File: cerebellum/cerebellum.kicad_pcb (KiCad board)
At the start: 2 copper layers, 91.5 x 52 mm, 82 parts, among them J1 PowerIn, J2 UART, J3 SWD_DBG, J4 SWD_DBG_PIN, J5 CAN FD, J6 CAN, Q1 AP2300, U1 OK1061-S, U2 TPS5430DDA, U3 BMI088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

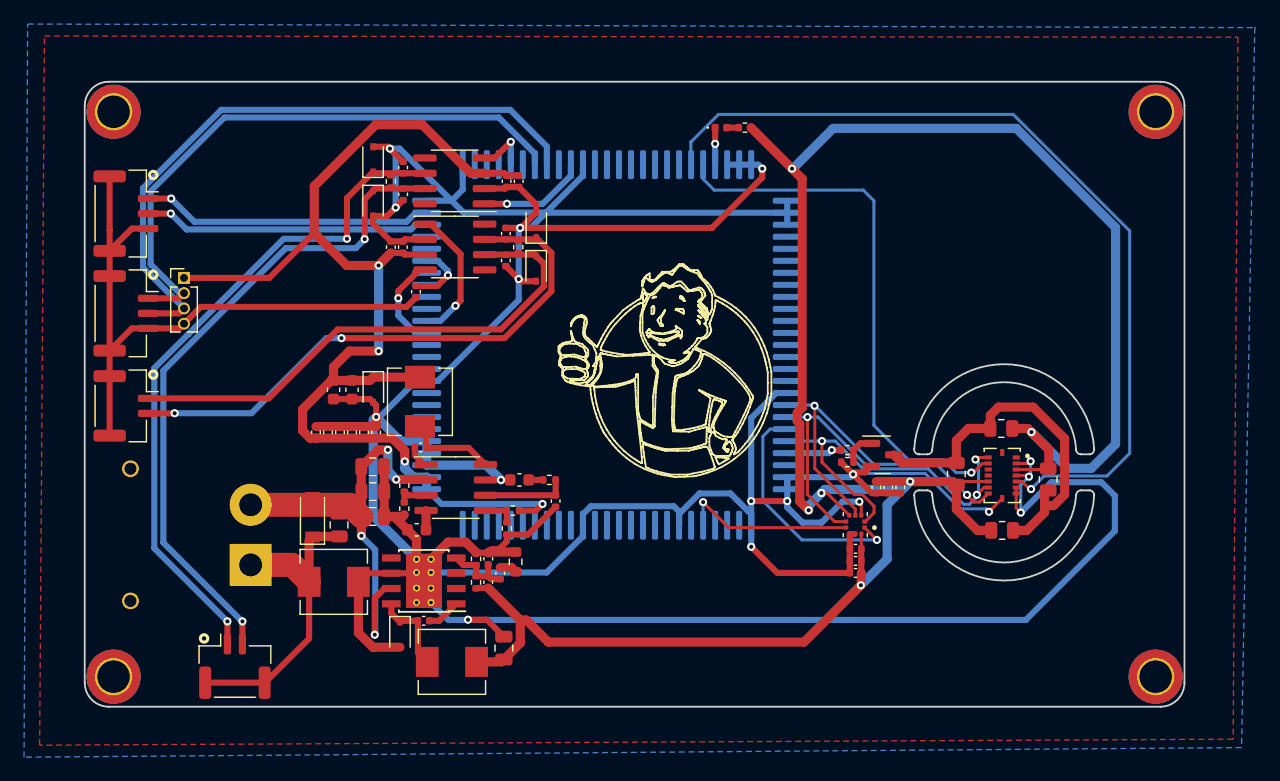
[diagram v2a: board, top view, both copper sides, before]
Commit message: [Modify] Replace DCDC(24to3V3) to LDO(5to3V3)
Signed-off-by: Homalozoa <nx.tardis@gmail.com>
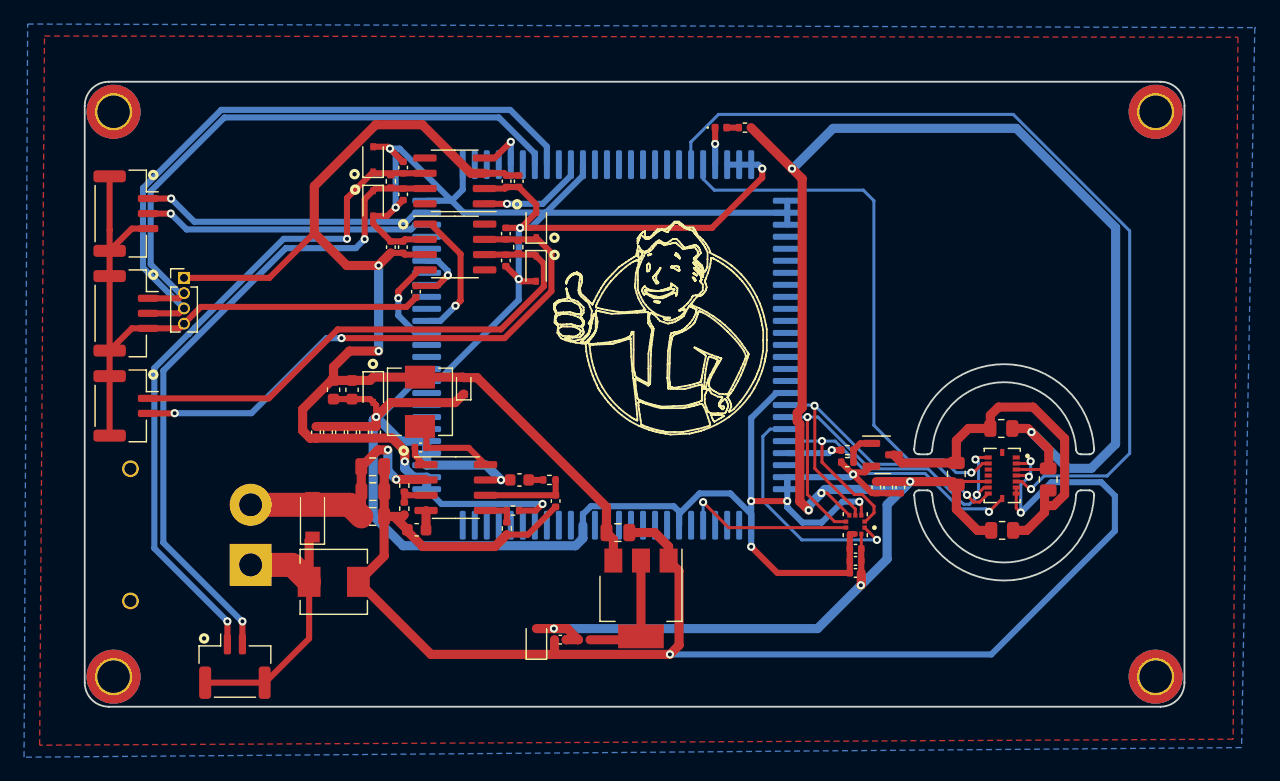
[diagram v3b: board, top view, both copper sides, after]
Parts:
- removed C19: 100uf/6.3V/0805, Capacitor_SMD:C_0805_2012Metric
- removed C21: 1.5nf/50V/0402, Capacitor_SMD:C_0402_1005Metric
- removed C24: 100nf/50V/0402, Capacitor_SMD:C_0402_1005Metric
- removed C28: 150pf/50V/0402, Capacitor_SMD:C_0402_1005Metric
- removed R11: 549R/0603, Resistor_SMD:R_0603_1608Metric
- removed R6: 10k/0402, Resistor_SMD:R_0402_1005Metric
- removed R7: 5.9k/0402, Resistor_SMD:R_0402_1005Metric
- added D9: PTVSLC3D3V3B, Diode_SMD:D_SOD-323, F.Cu at (141.8, 120.5)
- C13: value 4.7uF/50V/0805 -> 10uf/50V/0805
- C17: value 10nf/50V/0402 -> 22uf/6.3V/0402
- D2: value BZT52C3V3S -> TVSS5VCES-02GP; footprint Diode_SMD:D_SOD-323 -> Diode_SMD:D_SOD-523
- L2: value 15uh/SLO0530H150MTT -> MLG1005S1N3BT000; footprint Inductor_SMD:L_Sunlord_MWSA0518_5.4x5.2mm -> Inductor_SMD:L_0402_1005Metric
- U2: value TPS5430DDA -> AMS1117-3.3; footprint Package_SO:TI_SO-PowerPAD-8_ThermalVias -> Package_TO_SOT_SMD:SOT-223-3_TabPin2
- moved C13 23.2 mm to (148.6, 111.5), turned to 0 degrees
- moved D2 21.3 mm to (135.8, 99.3), turned to 90 degrees
- moved U2 18.1 mm to (150.5, 117.0), turned to -90 degrees
- moved C17 11.5 mm to (143.8, 120.4)
- moved L2 11.2 mm to (145.8, 120.4)
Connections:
- C13 pad 1: +24V -> +5V
- C13 pad 2: GNDA -> GND
- C17 pad 1: Net-(C17-Pad1) -> +3V3
- C17 pad 2: Net-(C17-Pad2) -> GND
- D2 pad 1: Net-(C17-Pad2) -> GND
- D2 pad 2: GND -> +5V
- L2 pad 1: +3V3 -> Net-(L2-Pad1)
- L2 pad 2: Net-(C17-Pad2) -> +3V3
- U2 pad 1: Net-(C17-Pad1) -> GND
- U2 pad 2: unconnected-(U2-Pad2) -> Net-(L2-Pad1)
- U2 pad 3: unconnected-(U2-Pad3) -> +5V
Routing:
- net +5V: track 99.2 -> 123.9 mm
- net GND: track 435.0 -> 453.1 mm
- net +24V: track 37.6 -> 22.6 mm, vias 4 -> 2
- net Net-(L2-Pad1): track 0.00 -> 10.7 mm
- net +3V3: track 185.6 -> 175.5 mm, vias 6 -> 7
- net Net-(C17-Pad2): track 6.95 -> 0.00 mm
- net TPS_VSEN: track 5.92 -> 0.00 mm
- net Net-(C17-Pad1): track 2.82 -> 0.00 mm
- net GNDA: track 26.4 -> 24.2 mm
- net Net-(C24-Pad2): track 1.43 -> 0.00 mm
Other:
- board text added: "Rev.v2"

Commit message: [Modify] Change pressure sensor to MPL3115A2R1
Signed-off-by: Homalozoa <nx.tardis@gmail.com>
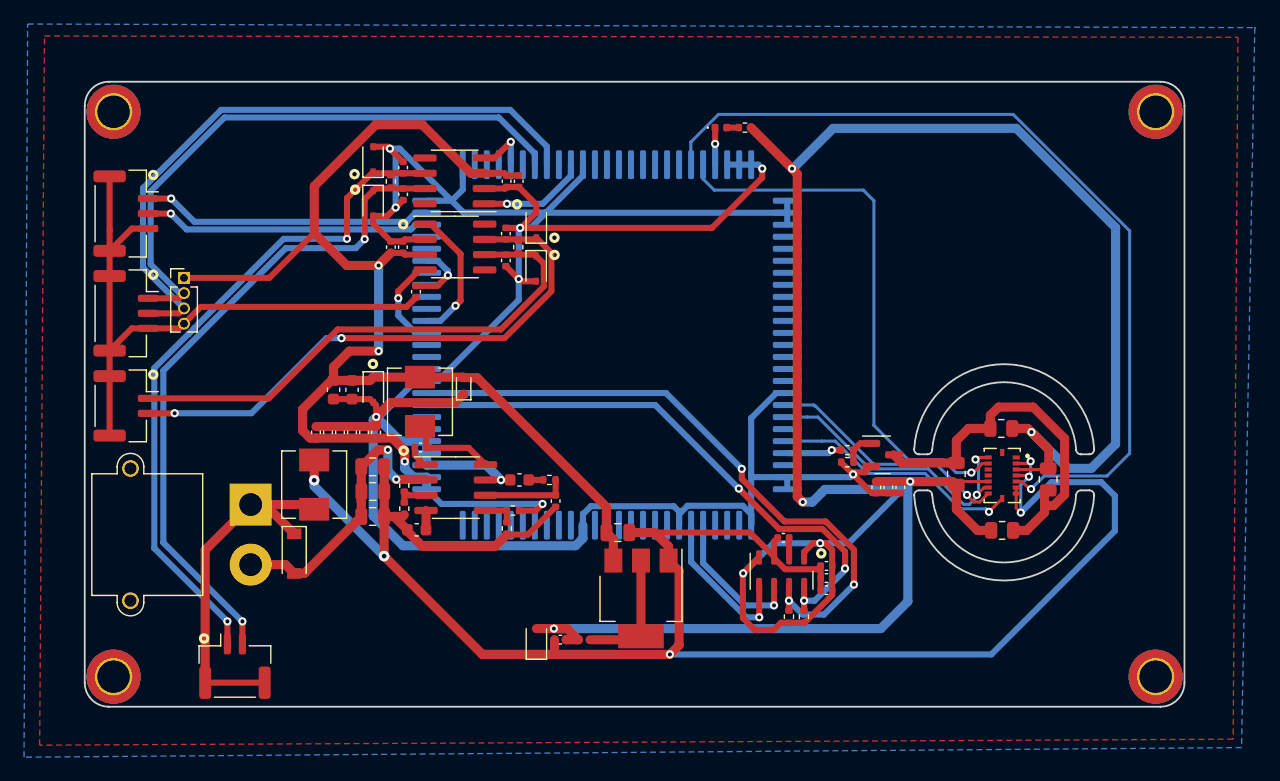
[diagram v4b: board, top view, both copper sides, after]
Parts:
- added C19: 100nF/10V/0402, Capacitor_SMD:C_0402_1005Metric, F.Cu at (162.4, 112.0)
- added R6: 1k/0402, Resistor_SMD:R_0402_1005Metric, F.Cu at (162.8, 118.5)
- added R7: 1k/0402, Resistor_SMD:R_0402_1005Metric, F.Cu at (164.1, 118.5)
- C31: value 4.7uF/10V/0402 -> 100nF/10V/0402
- C32: value 100nF/10V/0402 -> 1uF/10V/0402
- C51: value 100nF/10V/0402 -> 10uF/10V/0402
- J1: moved to F.Cu
- J2: value UART -> GH1.25-3PLTPZ
- J4: value SWD_DBG_PIN -> GH1.25-3PLTPZ
- J5: value CAN FD -> GH1.25-2PWBPZ
- J6: value CAN -> GH1.25-2PWBPZ
- U5: value ICP-20100 -> MPL3115A2; footprint Rolling_Custom:PQFN50P200X200X85-10N -> Package_LGA:NXP_LGA-8_3x5mm_P1.25mm_H1.1mm
- moved L3 8.25 mm to (123.3, 107.5), turned to -90 degrees
- moved U5 7.25 mm to (162.2, 114.7), turned to -90 degrees
- moved J1 5.02 mm to (118.1, 109.2), turned to 90 degrees
- moved D1 3.39 mm to (121.7, 113.3), turned to -90 degrees
- moved C31 2.81 mm to (166.0, 114.3)
- moved C32 2.81 mm to (166.0, 115.3)
- moved C51 2.81 mm to (166.0, 116.3)
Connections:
- U1 pad 70: ICP_SCS -> unconnected-(U1-Pad70)
- U1 pad 8: unconnected-(U1-Pad8) -> PRE_SDA
- U1 pad 80: ICP_INT -> PRE_INT1
- U1 pad 81: unconnected-(U1-Pad81) -> PRE_INT2
- U1 pad 9: unconnected-(U1-Pad9) -> PRE_SCL
- U5 pad 1: ICP_SCS -> +3V3
- U5 pad 2: SENSOR_SCK -> Net-(C19-Pad2)
- U5 pad 4: SENSOR_SDI -> +3V3
- U5 pad 5: +3V3 -> PRE_INT2
- U5 pad 6: SENSOR_SDO -> PRE_INT1
- U5 pad 7: ICP_INT -> PRE_SCL
- U5 pad 8: GND -> PRE_SDA
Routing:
- net PRE_SCL: track 0.00 -> 53.4 mm, vias 0 -> 3
- net PRE_SDA: track 0.00 -> 48.0 mm, vias 0 -> 3
- net +3V3: track 175.5 -> 208.8 mm
- net ICP_SCS: track 19.9 -> 0.00 mm, vias 1 -> 0
- net ICP_INT: track 14.7 -> 0.00 mm, vias 1 -> 0
- net PRE_INT2: track 0.00 -> 13.3 mm, vias 0 -> 1
- net PRE_INT1: track 0.00 -> 12.2 mm, vias 0 -> 1
- net SENSOR_SDO: track 35.2 -> 24.7 mm, vias 3 -> 2
- net SENSOR_SDI: track 30.9 -> 20.4 mm, vias 2 -> 1
- net SENSOR_SCK: track 30.0 -> 20.8 mm, vias 2 -> 1
- net GNDA: track 24.2 -> 31.4 mm
- net GND: track 453.1 -> 451.1 mm, vias 16 -> 14
- net +24V: track 22.6 -> 24.4 mm
- net Net-(C19-Pad2): track 0.00 -> 1.63 mm
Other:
- board text removed: "Rev.v2"
